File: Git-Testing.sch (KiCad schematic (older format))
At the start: 1 part

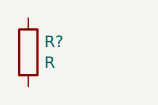
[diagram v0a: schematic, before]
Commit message: Added second resistor
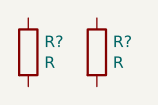
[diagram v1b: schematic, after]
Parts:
- added R?: R, symbol Device:R
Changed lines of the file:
@@
+	1    0    0    -1
+$EndComp
+$Comp
+L Device:R R?
+U 1 1 5F7E2506
+P 5600 2950
+F 0 "R?" H 5670 2996 50  0000 L CNN
+F 1 "R" H 5670 2905 50  0000 L CNN
+F 2 "" V 5530 2950 50  0001 C CNN
+F 3 "~" H 5600 2950 50  0001 C CNN
+	1    5600 2950
 	1    0    0    -1
 $EndComp
